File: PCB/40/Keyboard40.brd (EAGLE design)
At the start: 228.6 x 76.5 mm, 118 parts, among them J1 UX60SC-MB-5S8, SW1 TL3342F160QG/TR, U1 ATMEGA32U4-AUR, X1 FA-238

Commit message: Output files for 40
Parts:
- C6: value 4.7uF -> 1uF
- moved SW1 69.8 mm to (219.7, 60.3), turned to 180 degrees
- moved C8 29.9 mm to (209.6, 33.7), turned to 0 degrees
- moved R5 28.5 mm to (209.6, 63.5), turned to 0 degrees
- moved C6 26.0 mm to (178.4, 42.5), turned to 90 degrees
- moved X1 23.4 mm to (209.6, 38.1), turned to 270 degrees
- moved C7 22.8 mm to (209.6, 42.5), turned to 180 degrees
- moved C5 18.5 mm to (209.6, 60.3), turned to 180 degrees
- moved C1 17.5 mm to (209.6, 47.6), turned to 180 degrees
- moved C4 16.1 mm to (209.6, 57.1), turned to 180 degrees
- moved R6 15.9 mm to (178.4, 33.7), turned to 270 degrees
- moved C2 15.5 mm to (209.6, 50.8), turned to 180 degrees
- moved C3 15.0 mm to (209.6, 54.0), turned to 180 degrees
- moved R7 2.29 mm to (191.1, 59.1)
- moved U1 1.80 mm to (190.5, 38.1), turned to 270 degrees
- moved R8 0.90 mm to (195.6, 59.1)
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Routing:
- net COL3: track 183.9 -> 217.4 mm, vias 1 -> 3
- net COL0: track 312.6 -> 279.7 mm, vias 2 -> 3
- net COL6: track 209.6 -> 182.6 mm, vias 5 -> 3
- net N$9: track 72.6 -> 46.1 mm
- net COL5: track 258.0 -> 233.0 mm, vias 5 -> 3
- net ROW1: track 288.5 -> 264.3 mm, vias 5 -> 4
- net COL4: track 212.3 -> 235.2 mm, vias 0 -> 1
- net COL11: track 134.7 -> 111.9 mm, vias 2 -> 1
- net COL9: track 74.8 -> 94.4 mm
- net N$53: track 25.5 -> 5.93 mm
- net COL2: track 257.5 -> 238.9 mm, vias 3 -> 1
- net N$16: track 35.1 -> 20.6 mm, vias 0 -> 2
- net COL1: track 243.1 -> 228.9 mm, vias 3 -> 1
- net ROW0: track 287.2 -> 273.9 mm, vias 2 -> 3
- net N$10: track 19.6 -> 8.30 mm
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
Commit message: Cleanup. Add holes and use plate switches
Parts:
- U$1, U$10, U$11, U$12, U$16, U$17, U$18, U$19, U$2, U$20, U$21, U$22, U$23, U$24, U$25, U$26, U$27, U$28, U$29, U$3, U$30, U$31, U$32, U$33, U$34, U$35, U$36, U$37, U$38, U$39, U$4, U$40, U$41, U$42, U$43, U$44, U$45, U$46, U$47, U$48, U$49, U$5, U$50, U$51, U$6, U$7, U$8, U$9: value CHERRY_MX -> CHERRY_MXCHERRY_MX_PLATE; device CHERRY_MX:CHERRY_MX -> CHERRY_MX:CHERRY_MX_PLATE
- U$13, U$14, U$15: value CHERRY_MXCHERRY_MX_1_2 -> CHERRY_MXCHERRY_MX_1_2_PLATE; device CHERRY_MX:CHERRY_MX_1_2 -> CHERRY_MX:CHERRY_MX_1_2_PLATE
- moved D18 5.72 mm to (39.4, 10.8)
- moved C4 3.81 mm to (209.6, 61.0)
- moved C5 3.81 mm to (209.6, 64.1)
- moved R5 3.81 mm to (209.6, 67.3)
- moved D5 2.62 mm to (21.0, 52.1)
- moved D27 2.54 mm to (115.6, 33.0)
- moved D17 1.91 mm to (20.3, 14.6)
- moved D38 1.27 mm to (224.8, 72.4)
- moved D1 0.63 mm to (3.17, 72.4)
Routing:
- net ROW3: track 253.0 -> 261.1 mm
- net COL1: track 228.9 -> 235.1 mm
- net VCC: track 72.6 -> 78.7 mm
- net ROW2: track 248.6 -> 251.3 mm
- net N$21: track 6.79 -> 4.88 mm
- net N$2: track 5.72 -> 3.86 mm
- net COL0: track 279.7 -> 277.9 mm
- net N$9: track 46.1 -> 47.9 mm
- net N$45: track 11.8 -> 10.5 mm
- net N$38: track 4.46 -> 3.19 mm
- net ROW1: track 264.3 -> 265.3 mm
- net COL11: track 111.9 -> 111.2 mm

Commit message: Increase hole tolerance and round edges
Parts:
- moved D1 4.62 mm to (7.62, 73.7), turned to 0 degrees
- moved D38 1.91 mm to (224.8, 70.5)
- moved D17 0.63 mm to (20.3, 14.0)
- moved C1 0.63 mm to (209.6, 47.0)
- moved C2 0.63 mm to (209.6, 50.2)
- moved C3 0.63 mm to (209.6, 53.3)
- moved D5 0.63 mm to (21.0, 51.4)
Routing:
- net VCC: track 78.7 -> 80.7 mm
- net COL0: track 277.9 -> 276.1 mm
- net COL1: track 235.1 -> 236.7 mm
- net ROW0: track 273.7 -> 272.2 mm
- net ROW1: track 265.3 -> 266.7 mm
- net N$38: track 3.19 -> 4.49 mm
- net ROW3: track 261.1 -> 262.2 mm
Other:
- board size 228.6 x 76.5 mm -> 228.6 x 76.2 mm

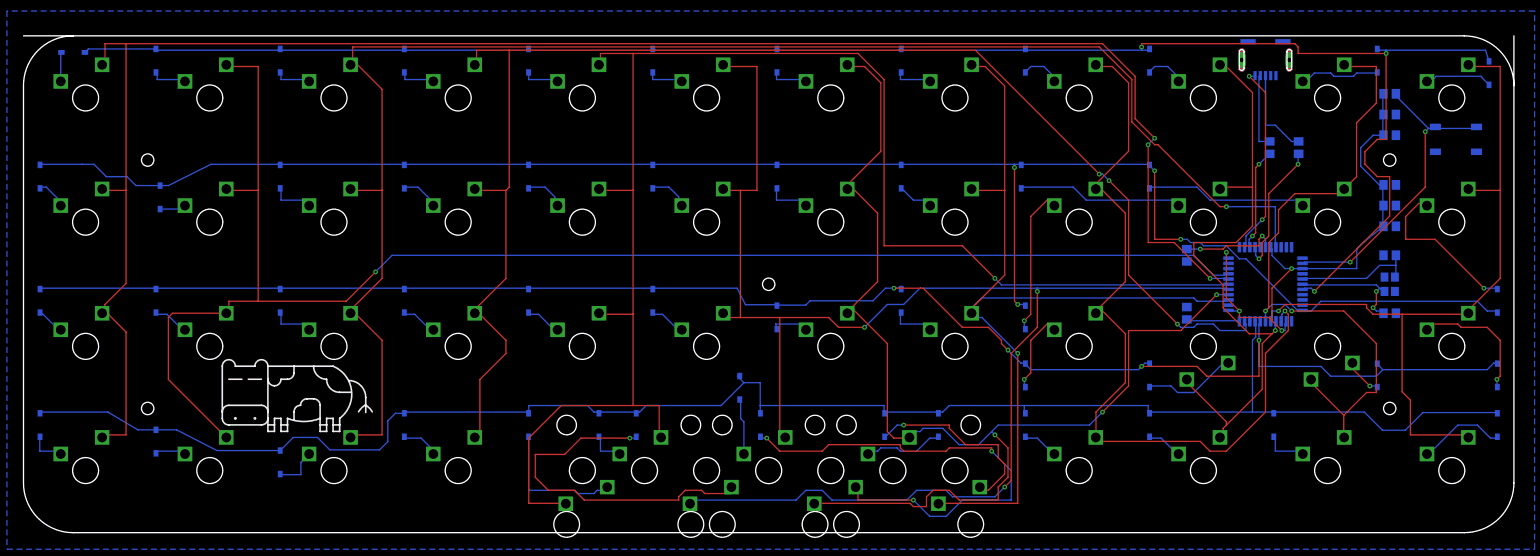
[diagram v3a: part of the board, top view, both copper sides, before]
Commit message: VUSB to VCC. Fix USB position
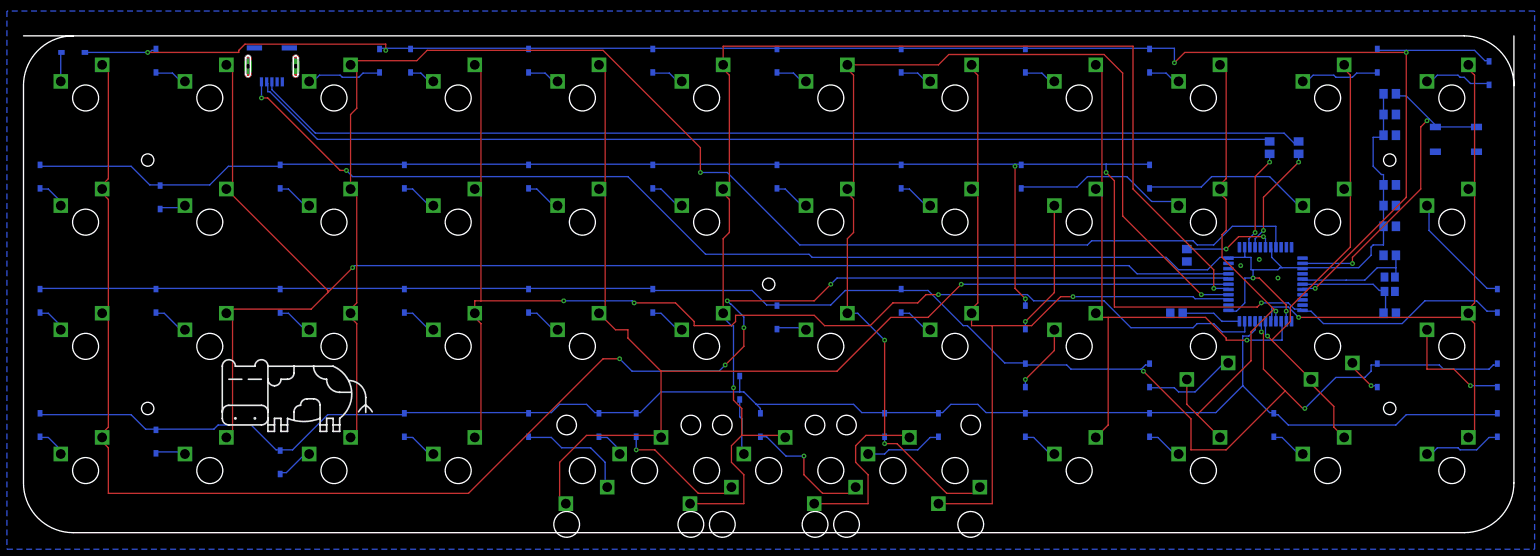
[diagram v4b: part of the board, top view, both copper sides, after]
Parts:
- moved J1 152.4 mm to (38.1, 75.2)
- moved D6 15.2 mm to (54.6, 72.4)
- moved R6 1.59 mm to (176.8, 33.7), turned to 180 degrees
- moved D7 0.95 mm to (59.4, 72.4)
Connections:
- removed net N$13: J1.1, U1.2
- net VCC: now also J1.1, U1.2
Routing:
- net VCC: track 80.7 -> 240.3 mm
- net N$17: track 13.7 -> 162.4 mm
- net N$15: track 11.9 -> 158.4 mm
- net N$41: track 74.8 -> 20.8 mm, vias 3 -> 1
- net COL4: track 235.2 -> 181.5 mm
- net COL5: track 233.0 -> 197.3 mm, vias 3 -> 2
- net N$40: track 53.8 -> 20.3 mm
- net N$13: track 29.7 -> 0.00 mm, vias 2 -> 0
- net COL3: track 217.4 -> 188.1 mm
- net COL10: track 100.3 -> 71.4 mm, vias 2 -> 1
- net COL8: track 121.2 -> 94.7 mm
- net COL11: track 111.2 -> 92.6 mm
- net COL9: track 94.4 -> 76.3 mm
- net COL2: track 238.9 -> 221.9 mm
- net COL7: track 134.9 -> 118.7 mm
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
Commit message: Holes for new case
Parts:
- moved D31 8.63 mm to (117.9, 9.41)
- moved D37 8.20 mm to (199.4, 72.4)
- moved D50 6.62 mm to (103.3, 21.3)
- moved D23 5.15 mm to (115.4, 49.5)
- moved D43 3.80 mm to (208.5, 27.8)
- moved R5 2.75 mm to (209.6, 70.1)
- moved C5 2.50 mm to (209.6, 66.6)
- moved C4 2.25 mm to (209.6, 63.2)
- moved D17 2.20 mm to (20.4, 11.8)
- moved D5 1.70 mm to (20.9, 49.7)
- moved C3 1.25 mm to (209.6, 52.1)
- moved C1 1.00 mm to (209.6, 46.0)
- moved C2 1.00 mm to (209.6, 49.2)
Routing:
- net ROW3: track 255.3 -> 275.5 mm
- net COL5: track 197.3 -> 212.1 mm
- net N$41: track 20.8 -> 10.4 mm, vias 1 -> 0
- net N$59: track 8.81 -> 18.8 mm
- net ROW0: track 273.4 -> 282.9 mm
- net N$51: track 12.3 -> 4.05 mm
- net ROW2: track 262.8 -> 269.9 mm
- net ROW1: track 281.4 -> 288.1 mm
- net VCC: track 240.3 -> 244.8 mm
- net N$17: track 162.4 -> 166.5 mm
- net N$15: track 158.4 -> 161.6 mm
- net COL2: track 221.9 -> 224.0 mm
- net N$9: track 49.5 -> 51.5 mm
- net N$53: track 5.84 -> 4.66 mm, vias 1 -> 0
- net N$2: track 4.15 -> 4.82 mm
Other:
- outline, holes or cut-outs redrawn
